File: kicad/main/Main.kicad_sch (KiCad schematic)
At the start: 0 parts

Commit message: Cliff/bumpers connector
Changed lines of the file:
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@@
 	(generator_version "10.0")
 	(paper "A2")
+	(rectangle
+		(start 374.65 247.65)
+		(end 464.82 375.92)
+		(stroke
+			(width 0)
+			(type solid)
+		)
+		(fill
+			(type color)
+			(color 0 72 0 1)
+		)
+	)
+	(rectangle
+		(start 245.11 135.89)
+		(end 463.55 149.86)
+		(stroke
+			(width 0)
+			(type solid)
+		)
+		(fill
+			(type color)
+			(color 0 72 0 1)
+		)
+	)
+	(rectangle
+		(start 66.04 73.66)
+		(end 180.34 303.53)
+		(stroke
+			(width 0)
+			(type solid)
+		)
+		(fill
+			(type color)
+			(color 0 72 0 1)
+		)
+	)
+	(rectangle
+		(start 180.34 217.17)
+		(end 199.39 242.57)
+		(stroke
+			(width 0)
+			(type solid)
+		)
+		(fill
+			(type color)
+			(color 0 72 0 1)
+		)
+	)
 	(text "IMU"
 		(exclude_from_sim no)
@@
 		)
 		(fill
-			(color 128 255 128 1)
+			(color 0 0 0 1)
 		)
 		(property "Sheetname" "CM5-HIGHSPEED"
@@
 		)
 		(fill
-			(color 128 255 128 1)
+			(color 0 0 0 1)
 		)
 		(property "Sheetname" "POWER"
@@
 		)
 		(fill
-			(color 128 255 128 1)
+			(color 0 0 0 1)
 		)
 		(property "Sheetname" "MAIN-FAN"
@@
 		)
 		(fill
-			(color 128 255 128 1)
+			(color 0 0 0 1)
 		)
 		(property "Sheetname" "CAMERA"
@@
 		)
 		(fill
-			(color 128 255 128 1)
+			(color 0 0 0 1)
 		)
 		(property "Sheetname" "SIDE-PROXI"
@@
 		)
 		(fill
-			(color 128 255 128 1)
+			(color 0 0 0 1)
 		)
 		(property "Sheetname" "MCU-STM32"
@@
 		)
 		(fill
-			(color 128 255 128 1)
+			(color 0 0 0 1)
 		)
 		(property "Sheetname" "IMU"
@@
 		)
 		(fill
-			(color 128 255 128 1)
+			(color 0 0 0 1)
 		)
 		(property "Sheetname" "SPEAKER-MIC"
@@
 		)
 		(fill
-			(color 128 255 128 1)
+			(color 0 0 0 1)
 		)
 		(property "Sheetname" "WATCHDOG"
@@
 		)
 		(fill
-			(color 128 255 128 1)
+			(color 0 0 0 1)
 		)
 		(property "Sheetname" "SIDE-BRUSH"
@@
 		)
 		(fill
-			(color 128 255 128 1)
+			(color 0 0 0 1)
 		)
 		(property "Sheetname" "LiDAR"
@@
 		)
 		(fill
-			(color 128 255 128 1)
+			(color 0 0 0 1)
 		)
 		(property "Sheetname" "FRONT SENSORS"
@@
 		)
 		(fill
-			(color 128 255 128 1)
+			(color 0 0 0 1)
 		)
 		(property "Sheetname" "M.2"
@@
 		)
 		(fill
-			(color 128 255 128 1)
+			(color 0 0 0 1)
 		)
 		(property "Sheetname" "MAIN-BRUSH MOTOR"
@@
 		)
 		(fill
-			(color 128 255 128 1)
+			(color 0 0 0 1)
 		)
 		(property "Sheetname" "WHEEL MOTOR"
@@
 		)
 		(fill
-			(color 128 255 128 1)
+			(color 0 0 0 1)
 		)
 		(property "Sheetname" "CM5-GPIO"
@@
 		)
 		(fill
-			(color 128 255 128 1)
+			(color 0 0 0 1)
 		)
 		(property "Sheetname" "ANTI-FALL"
@@
 		)
 		(fill
-			(color 128 255 128 1)
+			(color 0 0 0 1)
 		)
 		(property "Sheetname" "BUTTON-LED"
@@
 		)
 		(fill
-			(color 128 255 128 1)
+			(color 0 0 0 1)
 		)
 		(property "Sheetname" "BATTERY-CHARGER"
@@
 		)
 		(fill
-			(color 128 255 128 1)
+			(color 0 0 0 1)
 		)
 		(property "Sheetname" "WATER-PUMP"

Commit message: Second review round
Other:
- sheet ANTI-FALL renamed CLIFF
- added sheet CARPET-SENSOR (Carpet-sensor.kicad_sch)
- sheet CAMERA ports: added MIPI1_IO0, MIPI1_IO1; removed none
- sheet CLIFF: file ANTI-FALL-IR-SENSORs.kicad_sch -> CLIFF.kicad_sch
- sheet CM5-GPIO ports: added MIPI1_IO0, MIPI1_IO1; removed none
- sheet CM5-HIGHSPEED ports: added none; removed USB2_N, USB2_P
- sheet IMU ports: added IMU-SCL, IMU-SDA; removed IMU-SPI-CS, IMU-SPI-MISO, IMU-SPI-MOSI, IMU-SPI-SCLK
- sheet LiDAR ports: added LiDAR-EN; removed LIDAR_EN
- sheet MCU-STM32 ports: added 3.3V_JTG, CARPET-SENSOR-ECHO, CARPET-SENSOR-HI, CARPET-SENSOR-LO, DM, DP, I2C2_SCL, I2C2_SDA; removed IMU-SPI-CS, IMU-SPI-MISO, IMU-SPI-MOSI, IMU-SPI-SCLK, ~{JTAG_RST}
- sheet WATCHDOG ports: added ~{EN}; removed ~{MR}
- note added: "BATTERY CHARGER"
- note added: "CARPET-SENSOR"
- note added: "CLIFF"
- note removed: "ANTI-FALL IR"
- note removed: "CM5-HIGHSPEED"

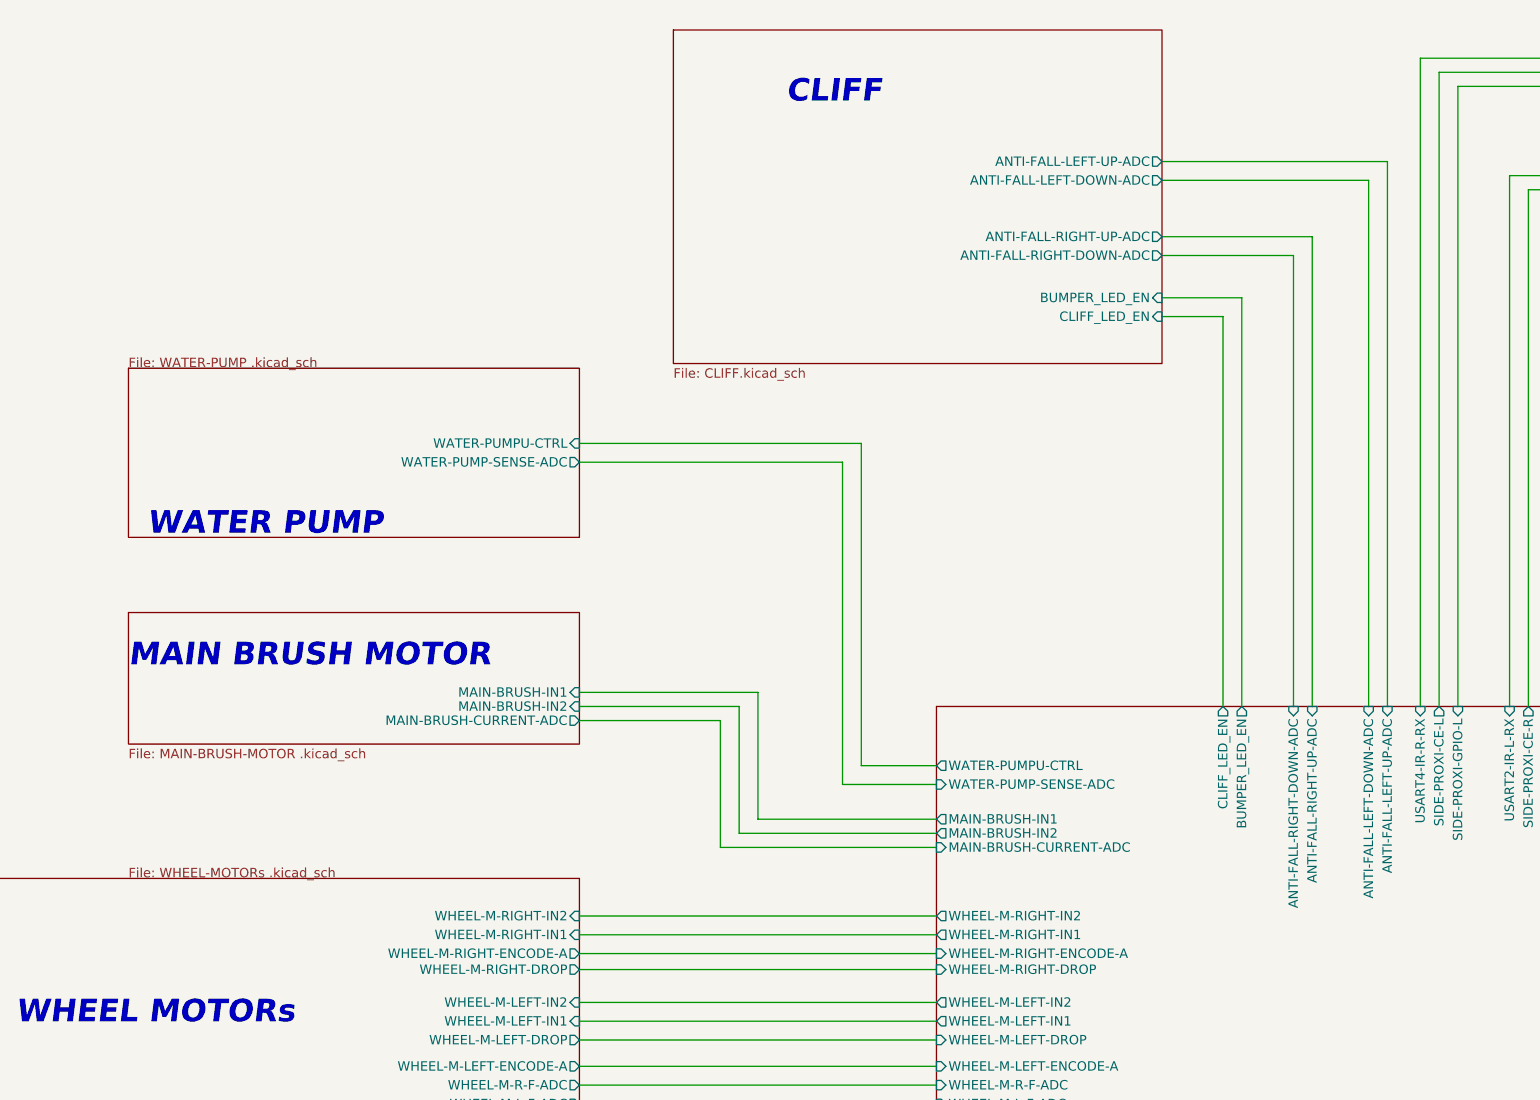
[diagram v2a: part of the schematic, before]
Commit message: Cliff/bumper connector reverse engineered
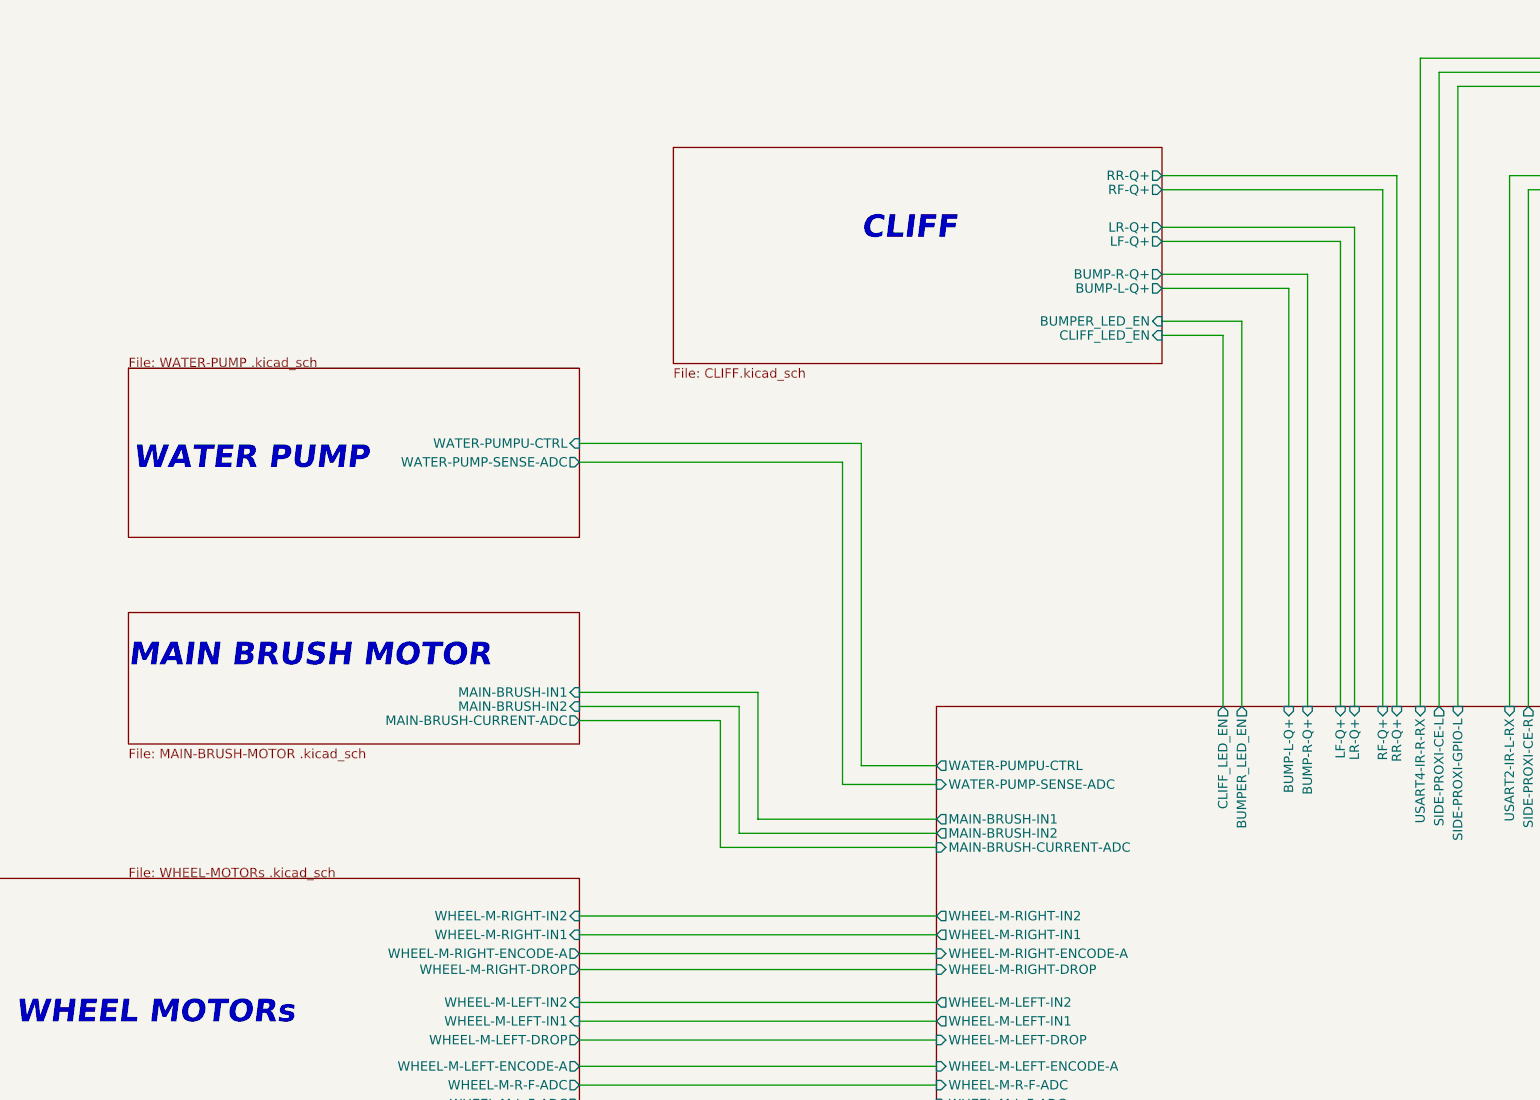
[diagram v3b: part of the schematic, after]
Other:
- sheet CLIFF ports: added BUMP-L-Q+, BUMP-R-Q+, LF-Q+, LR-Q+, RF-Q+, RR-Q+; removed ANTI-FALL-LEFT-DOWN-ADC, ANTI-FALL-LEFT-UP-ADC, ANTI-FALL-RIGHT-DOWN-ADC, ANTI-FALL-RIGHT-UP-ADC
- sheet MCU-STM32 ports: added BUMP-L-Q+, BUMP-R-Q+, LF-Q+, LR-Q+, RF-Q+, RR-Q+; removed ANTI-FALL-LEFT-DOWN-ADC, ANTI-FALL-LEFT-UP-ADC, ANTI-FALL-RIGHT-DOWN-ADC, ANTI-FALL-RIGHT-UP-ADC

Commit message: Add master fuse
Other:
- sheet MCU-STM32: file STM32G070RBT6.kicad_sch -> STM32G473.kicad_sch
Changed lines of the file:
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@@
 			)
 		)
-		(property "Sheetfile" "STM32G070RBT6.kicad_sch"
+		(property "Sheetfile" "STM32G473.kicad_sch"
 			(at 148.59 234.8996 0)
 			(show_name no)

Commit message: STM32 power rail switch
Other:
- sheet BATTERY-CHARGER ports: added PWR_EN; removed none
- sheet CM5-GPIO ports: added PI_DONE; removed none
- sheet MCU-STM32 ports: added 3.3V_EN, 5V_EN, PI_DONE, USB_PWR_EN; removed none
- sheet POWER ports: added 3.3V_EN, 5V_EN; removed none
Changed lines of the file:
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@@
 	(text "MAIN FAN"
 		(exclude_from_sim no)
-		(at 40.005 183.515 0)
+		(at 41.275 189.865 0)
 		(effects
 			(font
@@
 	(text "BATTERY CHARGER"
 		(exclude_from_sim no)
-		(at 248.92 323.215 0)
+		(at 248.92 351.155 0)
 		(effects
 			(font
@@
 	(text "POWER CONTROL"
 		(exclude_from_sim no)
-		(at 255.27 298.45 0)
+		(at 246.38 304.8 0)
 		(effects
 			(font
@@
 	(wire
 		(pts
+			(xy 262.89 218.44) (xy 306.07 218.44)
+		)
+		(stroke
+			(width 0)
+			(type default)
+		)
+	)
+	(wire
+		(pts
 			(xy 262.89 182.245) (xy 443.865 182.245)
 		)
@@
 	(wire
 		(pts
+			(xy 233.045 285.115) (xy 240.03 285.115)
+		)
+		(stroke
+			(width 0)
+			(type default)
+		)
+	)
+	(wire
+		(pts
 			(xy 394.97 367.03) (xy 443.865 367.03)
 		)
@@
 	(wire
 		(pts
-			(xy 226.695 321.31) (xy 226.695 234.315)
+			(xy 222.885 344.805) (xy 222.885 234.315)
 		)
 		(stroke
@@
 	(wire
 		(pts
-			(xy 240.03 285.115) (xy 217.17 285.115)
+			(xy 230.505 287.655) (xy 230.505 234.315)
 		)
 		(stroke
@@
 	(wire
 		(pts
-			(xy 233.045 315.595) (xy 240.665 315.595)
+			(xy 240.03 280.035) (xy 237.49 280.035)
+		)
+		(stroke
+			(width 0)
+			(type default)
+		)
+	)
+	(wire
+		(pts
+			(xy 227.965 340.995) (xy 240.665 340.995)
 		)
 		(stroke
@@
 	(wire
 		(pts
-			(xy 230.505 317.5) (xy 240.665 317.5)
+			(xy 225.425 342.9) (xy 240.665 342.9)
 		)
 		(stroke
@@
 	(wire
 		(pts
-			(xy 214.63 287.655) (xy 214.63 234.315)
+			(xy 235.585 282.575) (xy 235.585 234.315)
 		)
 		(stroke
@@
 	(wire
 		(pts
+			(xy 212.725 352.425) (xy 240.665 352.425)
+		)
+		(stroke
+			(width 0)
+			(type default)
+		)
+	)
+	(wire
+		(pts
 			(xy 239.395 53.34) (xy 239.395 114.3)
 		)
@@
 	(wire
 		(pts
-			(xy 219.71 234.315) (xy 219.71 330.835)
+			(xy 215.265 234.315) (xy 215.265 350.52)
 		)
 		(stroke
@@
 	(wire
 		(pts
-			(xy 230.505 234.315) (xy 230.505 317.5)
+			(xy 225.425 234.315) (xy 225.425 342.9)
 		)
 		(stroke
@@
 	(wire
 		(pts
-			(xy 224.155 234.315) (xy 224.155 323.85)
+			(xy 220.345 234.315) (xy 220.345 346.71)
 		)
 		(stroke
@@
 	(wire
 		(pts
+			(xy 212.725 234.315) (xy 212.725 352.425)
+		)
+		(stroke
+			(width 0)
+			(type default)
+		)
+	)
+	(wire
+		(pts
 			(xy 394.97 205.74) (xy 443.865 205.74)
 		)
@@
 	(wire
 		(pts
-			(xy 240.03 287.655) (xy 214.63 287.655)
+			(xy 240.03 282.575) (xy 235.585 282.575)
 		)
 		(stroke
@@
 	(wire
 		(pts
-			(xy 217.17 285.115) (xy 217.17 234.315)
+			(xy 240.03 287.655) (xy 230.505 287.655)
+		)
+		(stroke
+			(width 0)
+			(type default)
+		)
+	)
+	(wire
+		(pts
+			(xy 237.49 280.035) (xy 237.49 234.315)
 		)
 		(stroke
@@
 	(wire
 		(pts
-			(xy 226.695 321.31) (xy 240.665 321.31)
+			(xy 222.885 344.805) (xy 240.665 344.805)
+		)
+		(stroke
+			(width 0)
+			(type default)
+		)
+	)
+	(wire
+		(pts
+			(xy 233.045 234.315) (xy 233.045 285.115)
 		)
 		(stroke
@@
 	(wire
 		(pts
-			(xy 233.045 234.315) (xy 233.045 315.595)
+			(xy 227.965 234.315) (xy 227.965 340.995)
 		)
 		(stroke
@@
 	(wire
 		(pts
-			(xy 224.155 323.85) (xy 240.665 323.85)
+			(xy 220.345 346.71) (xy 240.665 346.71)
 		)
 		(stroke
@@
 	(wire
 		(pts
-			(xy 221.615 328.295) (xy 240.665 328.295)
+			(xy 217.805 348.615) (xy 240.665 348.615)
 		)
 		(stroke
@@
 	(wire
 		(pts
-			(xy 221.615 234.315) (xy 221.615 328.295)
+			(xy 217.805 234.315) (xy 217.805 348.615)
 		)
 		(stroke
@@
 	(wire
 		(pts
-			(xy 219.71 330.835) (xy 240.665 330.835)
+			(xy 215.265 350.52) (xy 240.665 350.52)
 		)
 		(stroke
@@
 	(sheet
 		(at 240.03 275.59)
-		(size 55.88 24.13)
+		(size 55.88 32.385)
 		(exclude_from_sim no)
 		(in_bom yes)
@@
 		)
 		(property "Sheetfile" "BMS-SYSTEM-POWER.kicad_sch"
-			(at 240.03 300.3046 0)
+			(at 240.03 308.5596 0)
 			(show_name no)
 			(do_not_autoplace no)
@@
 		)
 		(pin "PWR-BTN-SENSE" output
-			(at 240.03 287.655 180)
+			(at 240.03 282.575 180)
 			(effects
 				(font
@@
 		)
 		(pin "STM-PWR-CTRL" input
-			(at 240.03 285.115 180)
+			(at 240.03 280.035 180)
 			(effects
 				(font
@@
 			)
 		)
+		(pin "3.3V_EN" input
+			(at 240.03 285.115 180)
+			(effects
+				(font
+					(size 1.27 1.27)
+				)
+				(justify left)
+			)
+		)
+		(pin "5V_EN" input
+			(at 240.03 287.655 180)
+			(effects
+				(font
+					(size 1.27 1.27)
+				)
+				(justify left)
+			)
+		)
 		(instances
 			(project "Main"
@@
 	)
 	(sheet
-		(at 39.37 177.8)
-		(size 60.96 15.24)
+		(at 39.37 183.515)
+		(size 60.96 9.525)
 		(exclude_from_sim no)
 		(in_bom yes)
@@
 		)
 		(property "Sheetname" "MAIN-FAN"
-			(at 39.37 177.0884 0)
+			(at 39.37 182.8034 0)
 			(hide yes)
 			(show_name no)
@@
 		)
 		(pin "STM-PWR-CTRL" output
-			(at 217.17 234.315 270)
+			(at 237.49 234.315 270)
 			(effects
 				(font
@@
 		)
 		(pin "PWR-BTN-SENSE" input
-			(at 214.63 234.315 270)
+			(at 235.585 234.315 270)
 			(effects
 				(font
@@
 		)
 		(pin "BAT_ID" input
-			(at 224.155 234.315 270)
+			(at 220.345 234.315 270)
 			(effects
 				(font
@@
 		)
 		(pin "~{CHG_INT}" input
-			(at 226.695 234.315 270)
+			(at 222.885 234.315 270)
 			(effects
 				(font
@@
 		)
 		(pin "I2C3_SCL" output
-			(at 230.505 234.315 270)
+			(at 225.425 234.315 270)
 			(effects
 				(font
@@
 		)
 		(pin "I2C3_SDA" bidirectional
-			(at 233.045 234.315 270)
+			(at 227.965 234.315 270)
 			(effects
 				(font
@@
 		)
 		(pin "DM" bidirectional
-			(at 219.71 234.315 270)
+			(at 215.265 234.315 270)
 			(effects
 				(font
@@
 		)
 		(pin "DP" bidirectional
-			(at 221.615 234.315 270)
+			(at 217.805 234.315 270)
 			(effects
 				(font
@@
 			)
 		)
+		(pin "USB_PWR_EN" output
+			(at 212.725 234.315 270)
+			(effects
+				(font
+					(size 1.27 1.27)
+				)
+				(justify left)
+			)
+		)
+		(pin "3.3V_EN" output
+			(at 233.045 234.315 270)
+			(effects
+				(font
+					(size 1.27 1.27)
+				)
+				(justify left)
+			)
+		)
+		(pin "5V_EN" output
+			(at 230.505 234.315 270)
+			(effects
+				(font
+					(size 1.27 1.27)
+				)
+				(justify left)
+			)
+		)
+		(pin "PI_DONE" input
+			(at 262.89 218.44 0)
+			(effects
+				(font
+					(size 1.27 1.27)
+				)
+				(justify right)
+			)
+		)
 		(instances
 			(project "Main"
@@
 			)
 		)
+		(pin "PI_DONE" output
+			(at 306.07 218.44 180)
+			(effects
+				(font
+					(size 1.27 1.27)
+				)
+				(justify left)
+			)
+		)
 		(instances
 			(project "Main"
@@
 	)
 	(sheet
-		(at 240.665 310.896)
-		(size 55.245 24.384)
+		(at 240.665 338.836)
+		(size 55.245 18.669)
 		(exclude_from_sim no)
 		(in_bom yes)
@@
 		)
 		(property "Sheetname" "BATTERY-CHARGER"
-			(at 240.665 310.1844 0)
+			(at 240.665 338.1244 0)
 			(show_name no)
 			(do_not_autoplace no)
@@
 		)
 		(property "Sheetfile" "Battery-Charger.kicad_sch"
-			(at 240.665 335.8646 0)
+			(at 240.665 358.0896 0)
 			(show_name no)
 			(do_not_autoplace no)
@@
 		)
 		(pin "D+" bidirectional
-			(at 240.665 328.295 180)
+			(at 240.665 348.615 180)
 			(effects
 				(font
@@
 		)
 		(pin "D-" bidirectional
-			(at 240.665 330.835 180)
+			(at 240.665 350.52 180)
 			(effects
 				(font
@@
 		)
 		(pin "ID" output
-			(at 240.665 323.85 180)
+			(at 240.665 346.71 180)
 			(effects
 				(font
@@
 		)
 		(pin "SCL" input
-			(at 240.665 317.5 180)
+			(at 240.665 342.9 180)
 			(effects
 				(font
@@
 		)
 		(pin "SDA" bidirectional
-			(at 240.665 315.595 180)
+			(at 240.665 340.995 180)
 			(effects
 				(font
@@
 		)
 		(pin "~{INT}" output
-			(at 240.665 321.31 180)
+			(at 240.665 344.805 180)
+			(effects
+				(font
+					(size 1.27 1.27)
+				)
+				(justify left)
+			)
+		)
+		(pin "PWR_EN" input
+			(at 240.665 352.425 180)
 			(effects
 				(font

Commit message: LDR
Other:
- sheet CM5-GPIO ports: added PI_SHUTDOWN; removed none
- sheet MCU-STM32 ports: added PI_SHUTDOWN; removed none
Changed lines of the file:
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@@
 	(wire
 		(pts
+			(xy 262.89 215.9) (xy 306.07 215.9)
+		)
+		(stroke
+			(width 0)
+			(type default)
+		)
+	)
+	(wire
+		(pts
 			(xy 194.31 234.315) (xy 194.31 259.715)
 		)
@@
 			)
 		)
+		(pin "PI_SHUTDOWN" output
+			(at 262.89 215.9 0)
+			(effects
+				(font
+					(size 1.27 1.27)
+				)
+				(justify right)
+			)
+		)
 		(instances
 			(project "Main"
@@
 			(effects
 				(font
+					(size 1.27 1.27)
+				)
+				(justify left)
+			)
+		)
+		(pin "PI_SHUTDOWN" input
+			(at 306.07 215.9 180)
+			(effects
+				(font
